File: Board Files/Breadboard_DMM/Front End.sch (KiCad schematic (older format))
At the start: 13 parts, among them J401 V+, J402 I+, J403 COM, K2 EC2-5NU, K3 EC2-5NU, U401 LMV358

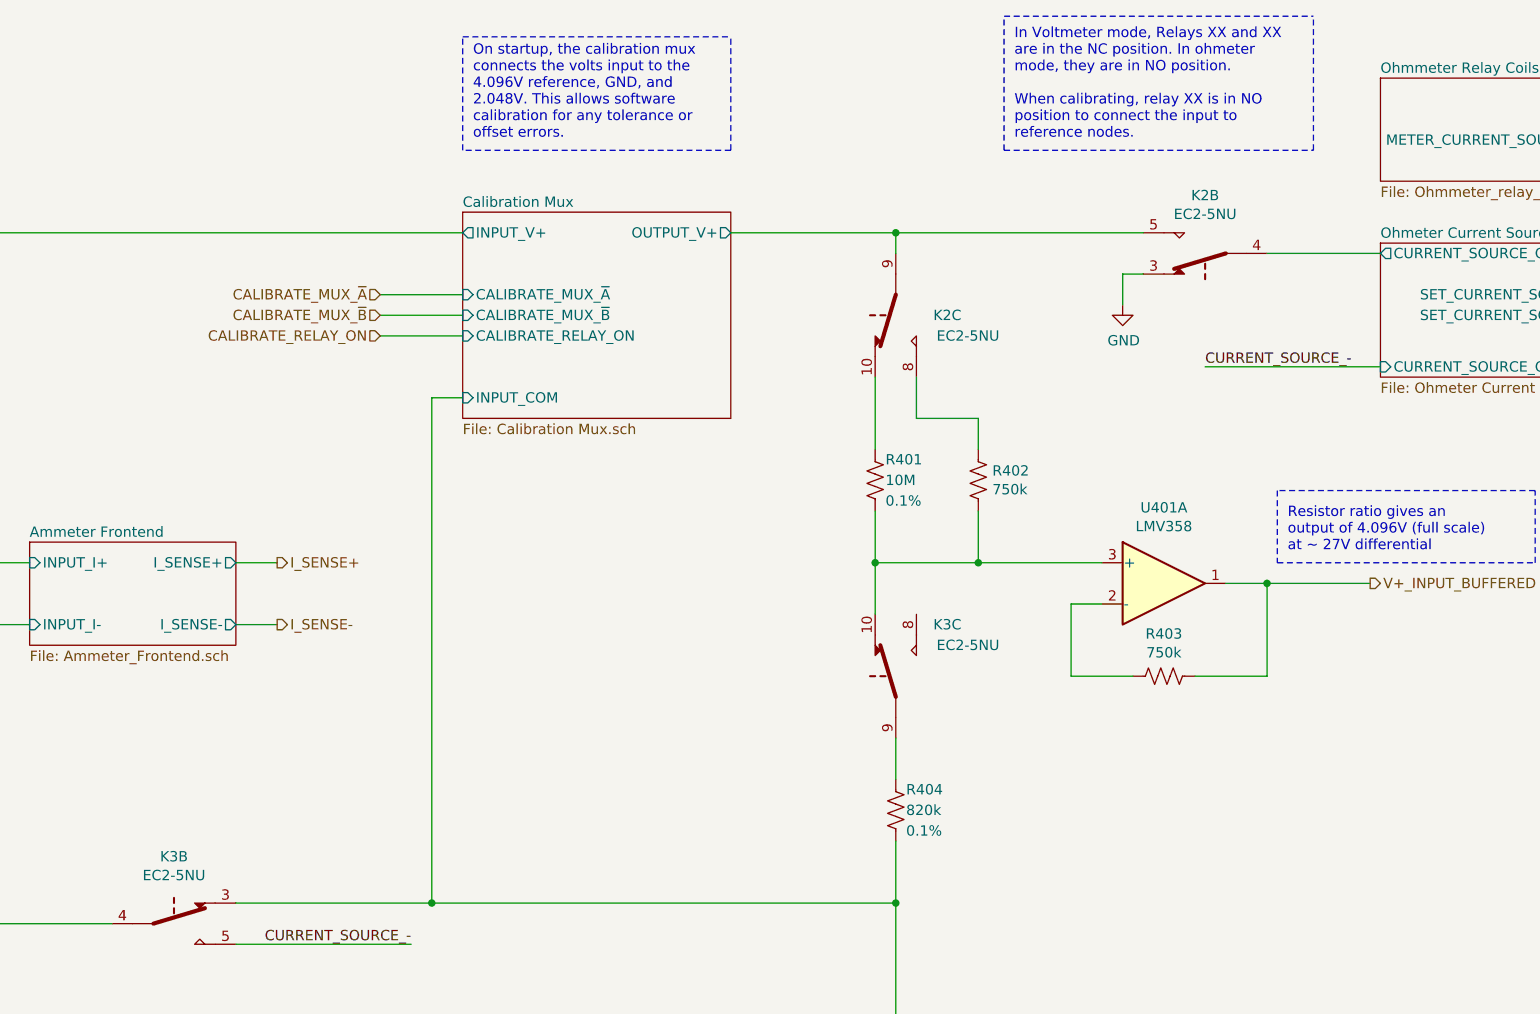
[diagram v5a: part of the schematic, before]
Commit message: Started adding Digikey links
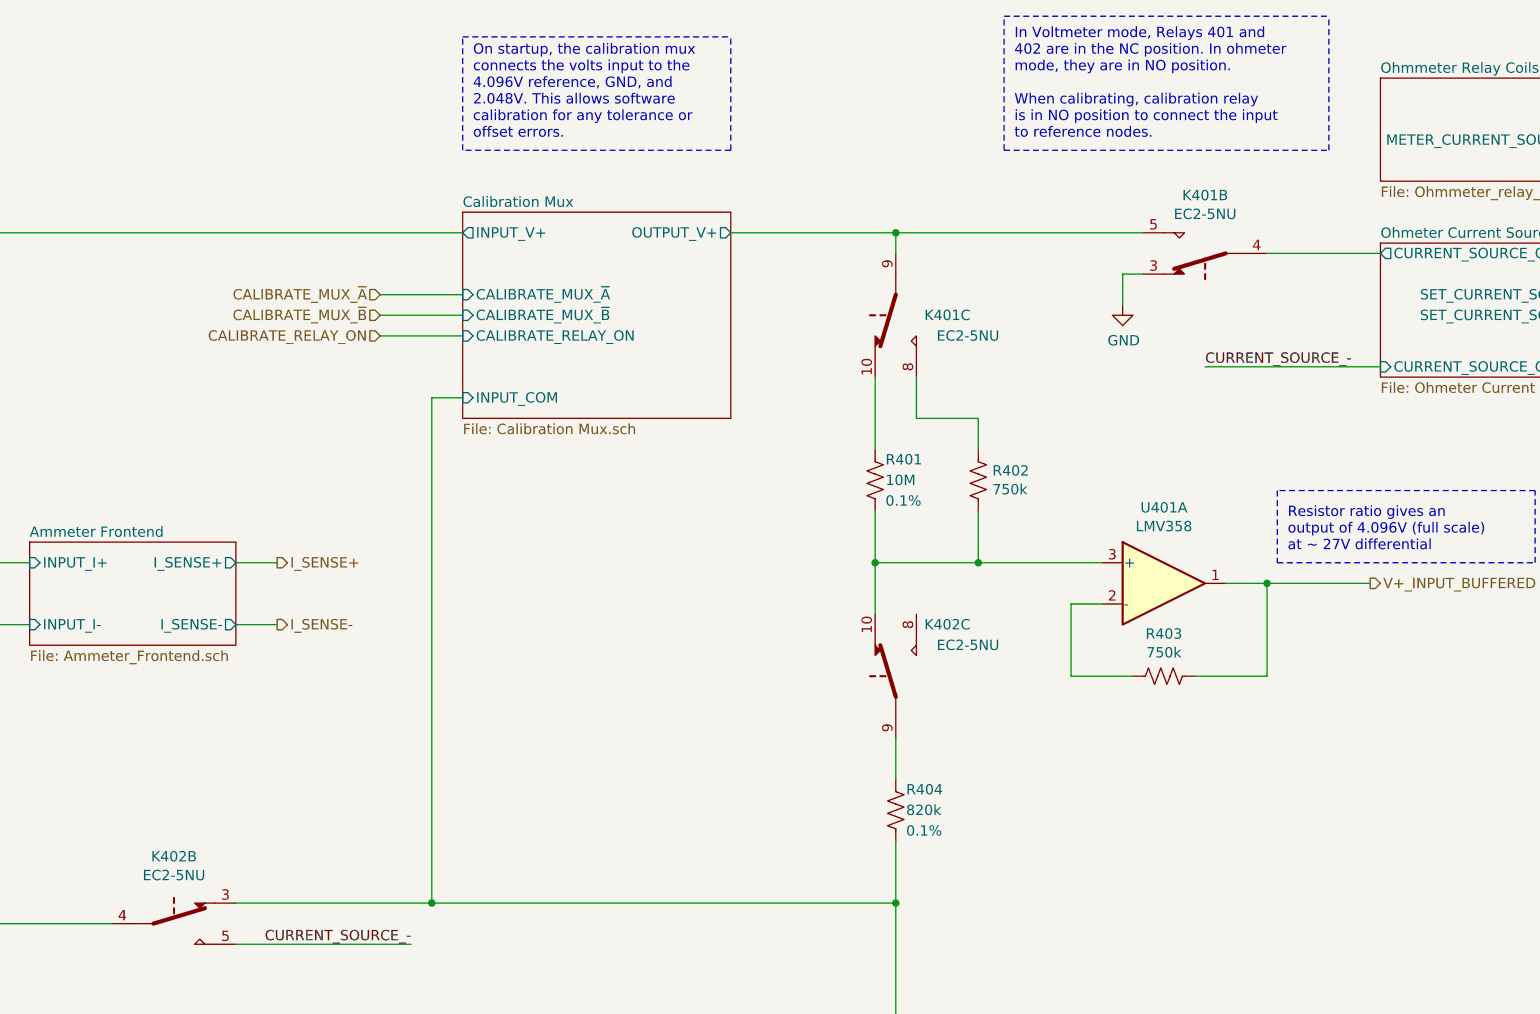
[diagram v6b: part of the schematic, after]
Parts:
- renumbered K2 to K401, K3 to K402
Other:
- note added: "In Voltmeter mode, Relays 401 and \n402 are in the NC position. In ohmeter\nmode, they are in NO position. \n\nWhen calibrating, calibration relay \nis in NO position to connect the input\nto reference nodes."
- note removed: "In Voltmeter mode, Relays XX and XX\nare in the NC position. In ohmeter\nmode, they are in NO position. \n\nWhen calibrating, relay XX is in NO\nposition to connect the input to \nreference nodes."
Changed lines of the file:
@@
 $Descr USLetter 11000 8500
 encoding utf-8
-Sheet 4 10
+Sheet 4 11
 Title "Toast-O-Meter"
-Date ""
+Date "2020-08-14"
 Rev "0"
 Comp ""
@@
 P 7050 2100
 AR Path="/5F56935A" Ref="K?"  Part="2"
-AR Path="/5F511849/5F56935A" Ref="K2"  Part="2"
-F 0 "K2" V 7331 2100 50  0000 C CNN
+AR Path="/5F511849/5F56935A" Ref="K401"  Part="2"
+F 0 "K401" V 7331 2100 50  0000 C CNN
 F 1 "EC2-5NU" V 7240 2100 50  0000 C CNN
 F 2 "Relay_THT:Relay_DPDT_Kemet_EC2" H 7250 2000 50  0001 L CNN
@@
 P 5550 4150
 AR Path="/5F56933F" Ref="K?"  Part="3"
-AR Path="/5F511849/5F56933F" Ref="K3"  Part="3"
-F 0 "K3" H 5800 4400 50  0000 C CNN
+AR Path="/5F511849/5F56933F" Ref="K402"  Part="3"
+F 0 "K402" H 5800 4400 50  0000 C CNN
 F 1 "EC2-5NU" H 5900 4300 50  0000 C CNN
 F 2 "Relay_THT:Relay_DPDT_Kemet_EC2" H 5750 4050 50  0001 L CNN
@@
 Connection ~ 7350 3700
 Text Notes 6125 1550 0    50   ~ 0
-In Voltmeter mode, Relays XX and XX\nare in the NC position. In ohmeter\nmode, they are in NO position. \n\nWhen calibrating, relay XX is in NO\nposition to connect the input to \nreference nodes.
+In Voltmeter mode, Relays 401 and \n402 are in the NC position. In ohmeter\nmode, they are in NO position. \n\nWhen calibrating, calibration relay \nis in NO position to connect the input\nto reference nodes.
 Text HLabel 7850 3700 2    50   Output ~ 0
 V+_INPUT_BUFFERED
@@
 	8650 3250 7400 3250
 Wire Notes Line width 8 style solid
-	6075 1600 7575 1600
-Wire Notes Line width 8 style solid
-	7575 1600 7575 950
-Wire Notes Line width 8 style solid
-	6075 950  7575 950
+	6075 1600 7650 1600
+Wire Notes Line width 8 style solid
+	7650 1600 7650 950
+Wire Notes Line width 8 style solid
+	6075 950  7650 950
 Wire Notes Line width 8 style solid
 	6075 1600 6075 950
@@
 P 2050 5350
 AR Path="/5F569339" Ref="K?"  Part="2"
-AR Path="/5F511849/5F569339" Ref="K3"  Part="2"
-F 0 "K3" V 1725 5350 50  0000 C CNN
+AR Path="/5F511849/5F569339" Ref="K402"  Part="2"
+F 0 "K402" V 1725 5350 50  0000 C CNN
 F 1 "EC2-5NU" V 1816 5350 50  0000 C CNN
 F 2 "Relay_THT:Relay_DPDT_Kemet_EC2" H 2250 5250 50  0001 L CNN
@@
 P 5550 2400
 AR Path="/5F569360" Ref="K?"  Part="3"
-AR Path="/5F511849/5F569360" Ref="K2"  Part="3"
-F 0 "K2" H 5800 2400 50  0000 C CNN
+AR Path="/5F511849/5F569360" Ref="K401"  Part="3"
+F 0 "K401" H 5800 2400 50  0000 C CNN
 F 1 "EC2-5NU" H 5900 2500 50  0000 C CNN
 F 2 "Relay_THT:Relay_DPDT_Kemet_EC2" H 5750 2300 50  0001 L CNN

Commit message: Finished adding parts, cleaned up, ran ERC
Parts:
- removed J401: V+, symbol Connector_Generic:Conn_01x01
- removed J402: I+, symbol Connector_Generic:Conn_01x01
- removed J403: COM, symbol Connector_Generic:Conn_01x01
- added D401, D402: 1N4007, Diode_SMD:D_SOD-123, symbol Device:D_ALT
- added J401: V+, Connector_PinHeader_2.54mm:PinHeader_1x02_P2.54mm_Vertical, symbol Connector_Generic:Conn_01x02
- added J402: I+, Connector_PinHeader_2.54mm:PinHeader_1x02_P2.54mm_Vertical, symbol Connector_Generic:Conn_01x02
- added J403: COM, Connector_PinHeader_2.54mm:PinHeader_1x02_P2.54mm_Vertical, symbol Connector_Generic:Conn_01x02
- added unit 1 of K401
- added unit 1 of K402
- added Q401: NTZD3154N, Package_TO_SOT_SMD:SOT-563, symbol irex_Transistor_FET:NTZD3154N
- added R407, R408: 100, Resistor_SMD:R_0603_1608Metric_Pad1.05x0.95mm_HandSolder, symbol Device:R_US
- added R409, R410: 10k, Resistor_SMD:R_0603_1608Metric_Pad1.05x0.95mm_HandSolder, symbol Device:R_US
- C401: footprint (none) -> Resistor_SMD:R_0603_1608Metric_Pad1.05x0.95mm_HandSolder; Digi-Key Link (none) -> https://www.digikey.com/en/products/detail/samsung-electro-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; Digi-Key PN - -> 1276-6524-1-ND
- K401, K402: Digi-Key Link (none) -> https://www.digikey.com/en/products/detail/kemet/EC2-5NU/42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; Digi-Key PN - -> 399-11052-5-ND
- R401: footprint (none) -> Resistor_SMD:R_0603_1608Metric_Pad1.05x0.95mm_HandSolder; Digi-Key Link (none) -> https://www.digikey.com/en/products/detail/vishay-dale/CRCW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; Digi-Key PN - -> 541-10MAYCT-ND; Tolerance 0.1% -> 0.5%
- R402, R403: footprint (none) -> Resistor_SMD:R_0603_1608Metric_Pad1.05x0.95mm_HandSolder; Digi-Key Link (none) -> https://www.digikey.com/en/products/detail/yageo/RC0603FR-0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; Digi-Key PN - -> 311-750KHRCT-ND
- R404: footprint (none) -> Resistor_SMD:R_0805_2012Metric_Pad1.15x1.40mm_HandSolder; Digi-Key Link (none) -> https://www.digikey.com/en/products/detail/yageo/RT0805BRD0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; Digi-Key PN - -> YAG1978CT-ND
- R405, R406: footprint (none) -> Resistor_SMD:R_0603_1608Metric_Pad1.05x0.95mm_HandSolder; Digi-Key Link (none) -> https://www.digikey.com/en/products/detail/yageo/RC0603FR-0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; Digi-Key PN - -> 311-10.0KHRCT-ND
- U401: footprint (none) -> Package_SO:SOIC-8_3.9x4.9mm_P1.27mm; Digi-Key Link (none) -> https://www.digikey.com/en/products/detail/texas-instrument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; Digi-Key PN - -> 296-47593-1-ND
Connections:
- net +5VA: now also D401.1 (K), D402.1 (K), K401.1, K402.1
- net Ammeter Frontend/INPUT_I+: now also J402.1 (Pin_1), J402.2 (Pin_2)
- net Ammeter Frontend/INPUT_I-: now also J403.1 (Pin_1), J403.2 (Pin_2)
- net Calibration Mux/INPUT_V+: now also J401.1 (Pin_1), J401.2 (Pin_2)
- net GND: now also Q401.1 (S1), Q401.4 (S2), R409.2, R410.2
- net METER_CURRENT_SOURCE_ON: now also R407.1, R408.1
- new net: Q401.2 (G1), R407.2, R409.1
- new net: D401.2 (A), K401.12, Q401.6 (D1)
- new net: Q401.5 (G2), R408.2, R410.1
- new net: D402.2 (A), K402.12, Q401.3 (D2)
- no-connect marks 0 -> 1
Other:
- note added: "Ohmmeter Relay Coils"
- moved on the sheet: C401, K401B, K401C, K402B, K402C, R401, R402, R403, R404, R405, R406, U401A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

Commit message: Cleaned up files
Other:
- note added: "Sheet 4"
- note added: "Sheet 5"
- note added: "Sheet 6"
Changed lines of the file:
@@
 Wire Notes Line width 8 style solid
 	8575 1650 8575 1000
-Text HLabel 12450 2550 2    50   Input ~ 0
+Text HLabel 12950 2550 2    50   Input ~ 0
 SET_CURRENT_SOURCE_B
-Text HLabel 12450 2450 2    50   Input ~ 0
+Text HLabel 12950 2450 2    50   Input ~ 0
 SET_CURRENT_SOURCE_A
 $Sheet
-S 10950 2200 1150 650
+S 10950 2200 1650 700
 U 5F7E68F4
 F0 "Ohmeter Current Source" 50
 F1 "Ohmeter Current Source.sch" 50
-F2 "SET_CURRENT_SOURCE_A" I R 12100 2450 50
-F3 "SET_CURRENT_SOURCE_B" I R 12100 2550 50
+F2 "SET_CURRENT_SOURCE_A" I R 12600 2450 50
+F3 "SET_CURRENT_SOURCE_B" I R 12600 2550 50
 F4 "CURRENT_SOURCE_OUT+" O L 10950 2250 50
 F5 "CURRENT_SOURCE_OUT-" I L 10950 2800 50
 $EndSheet
 Wire Wire Line
-	12450 2550 12100 2550
-Wire Wire Line
-	12450 2450 12100 2450
-Wire Wire Line
 	9700 2250 10950 2250
 $Sheet
-S 5100 2050 1300 1000
+S 5100 2050 1600 1000
 U 5F4FBB9F
 F0 "Calibration Mux" 50
@@
 F5 "CALIBRATE_MUX_~B" I L 5100 2550 50
 F6 "CALIBRATE_RELAY_ON" I L 5100 2650 50
-F7 "OUTPUT_V+" O R 6400 2150 50
+F7 "OUTPUT_V+" O R 6700 2150 50
 $EndSheet
 Wire Wire Line
@@
 Wire Wire Line
 	7700 2900 7700 3200
-Wire Wire Line
-	7600 2150 9100 2150
-Connection ~ 7600 2150
-Wire Wire Line
-	7600 2300 7600 2150
 $Comp
 L irex_Relay:EC2-5NU_Split K?
@@
 $EndComp
 Wire Wire Line
-	6400 2150 7600 2150
-Wire Wire Line
 	7500 2900 7500 3500
 Wire Wire Line
@@
 $EndComp
 $Sheet
-S 2600 4250 1000 500
+S 2450 4250 1100 650
 U 5FE469BC
 F0 "Ammeter Frontend" 50
 F1 "Ammeter_Frontend.sch" 50
-F2 "I_SENSE-" O R 3600 4650 50
-F3 "I_SENSE+" O R 3600 4350 50
-F4 "INPUT_I+" I L 2600 4350 50
-F5 "INPUT_I-" I L 2600 4650 50
+F2 "I_SENSE-" O R 3550 4800 50
+F3 "I_SENSE+" O R 3550 4350 50
+F4 "INPUT_I+" I L 2450 4350 50
+F5 "INPUT_I-" I L 2450 4800 50
 $EndSheet
 Wire Wire Line
-	2600 4650 2400 4650
-Wire Wire Line
-	2400 4650 2400 6600
-Wire Wire Line
-	2400 6600 3400 6600
-Wire Wire Line
-	3600 4350 3800 4350
-Wire Wire Line
-	3600 4650 3800 4650
-Text HLabel 3800 4350 2    50   Output ~ 0
+	2450 4800 2250 4800
+Wire Wire Line
+	2250 4800 2250 6600
+Wire Wire Line
+	2250 6600 3400 6600
+Text HLabel 3750 4350 2    50   Output ~ 0
 I_SENSE+
-Text HLabel 3800 4650 2    50   Output ~ 0
+Text HLabel 3750 4800 2    50   Output ~ 0
 I_SENSE-
 Wire Wire Line
@@
 	1700 4400 1650 4400
 Wire Wire Line
-	1700 4350 2600 4350
+	1700 4350 2450 4350
 Connection ~ 1700 4350
 Wire Wire Line
@@
 	1700 6650 1650 6650
 Wire Wire Line
-	1700 6600 2400 6600
+	1700 6600 2250 6600
 Connection ~ 1700 6600
 Wire Wire Line
 	1700 6600 1700 6650
-Connection ~ 2400 6600
+Connection ~ 2250 6600
 NoConn ~ 7700 4550
 Text HLabel 15150 6250 2    50   Input ~ 0
@@
 	1    0    0    -1
 $EndComp
+Wire Wire Line
+	7600 2300 7600 2150
+Connection ~ 7600 2150
+Wire Wire Line
+	7600 2150 9100 2150
+Wire Wire Line
+	3550 4350 3750 4350
+Wire Wire Line
+	3750 4800 3550 4800
+Text Notes 2950 4150 0    100  ~ 20
+Sheet 6
+Text Notes 6100 2000 0    100  ~ 20
+Sheet 5
+Text Notes 12000 2100 0    100  ~ 20
+Sheet 4
+Wire Wire Line
+	6700 2150 7600 2150
+Wire Wire Line
+	12600 2550 12950 2550
+Wire Wire Line
+	12600 2450 12950 2450
 $EndSCHEMATC
